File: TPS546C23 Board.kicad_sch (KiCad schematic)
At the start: 35 parts, among them IC1 TPS546C23RVFT

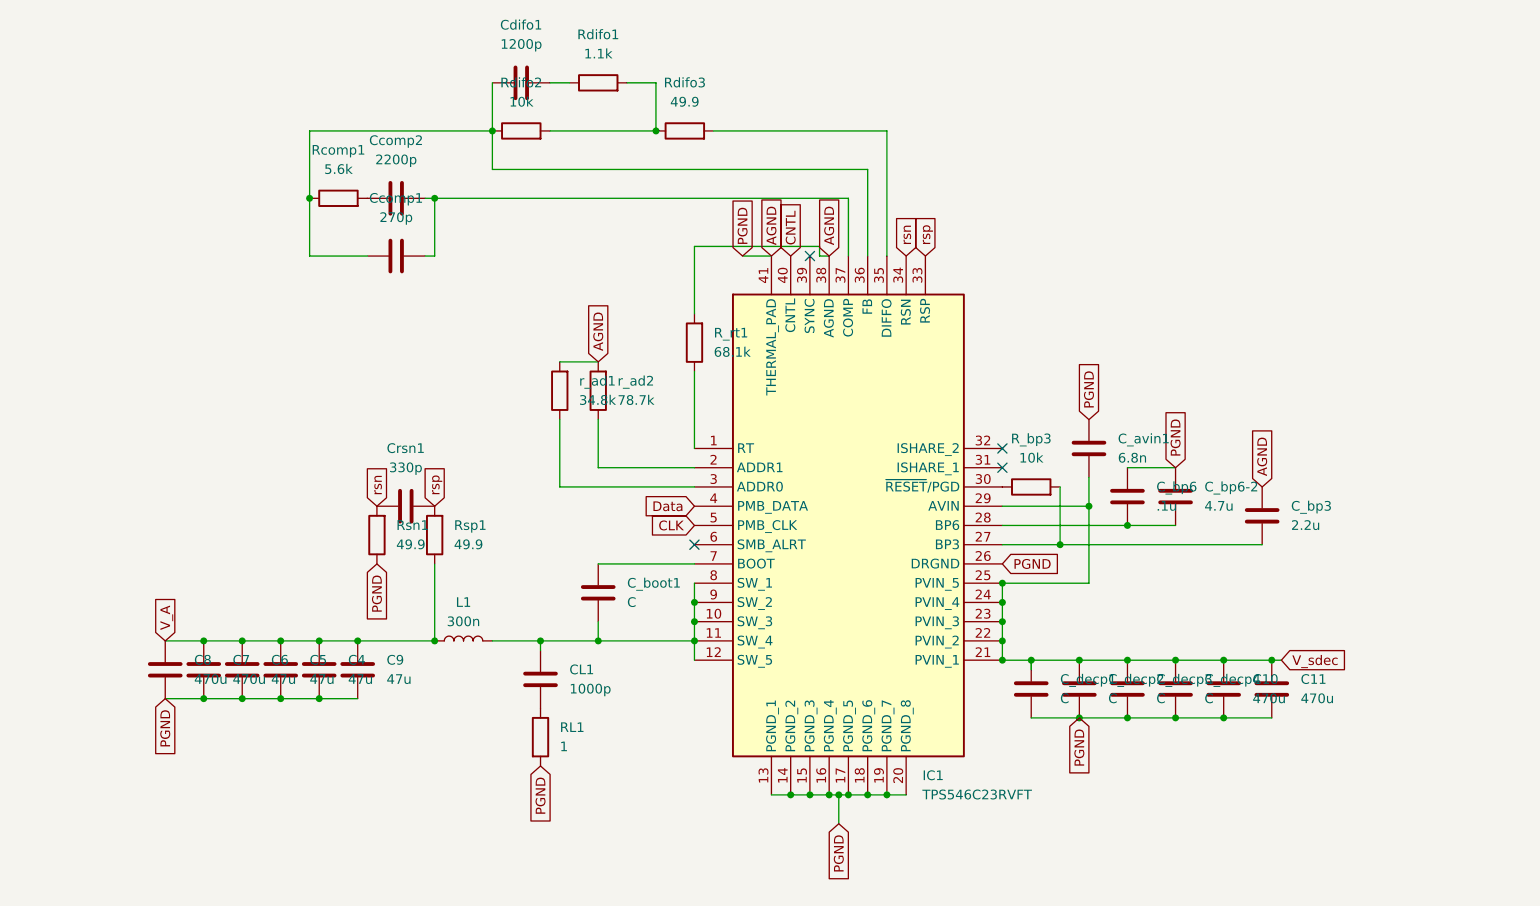
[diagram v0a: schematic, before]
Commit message: add fp and sym, it wasnt final
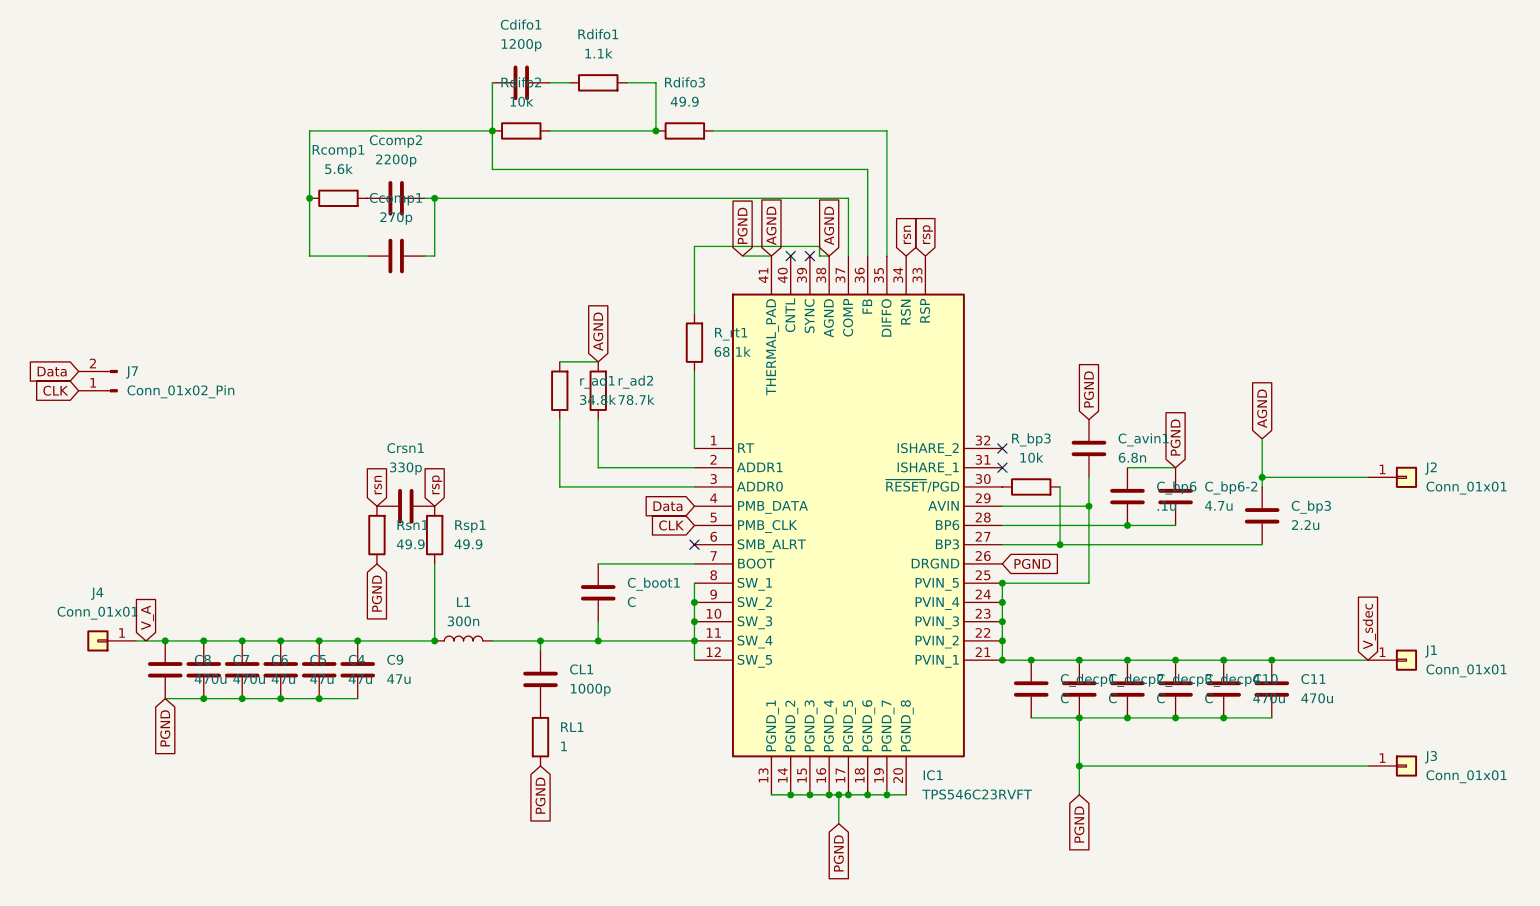
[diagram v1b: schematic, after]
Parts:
- added J1, J2, J3, J4: Conn_01x01, Custom:CalTest_CT3151, symbol Connector_Generic:Conn_01x01
- added J7: Conn_01x02_Pin, Connector_PinHeader_2.54mm:PinHeader_1x02_P2.54mm_Vertical, symbol Connector:Conn_01x02_Pin
- IC1: footprint LIB_TPS546C23RVFT:QFN50P500X700X152-41N-D -> Custom:QFN50P500X700X152-41N-D; symbol highA_highV_buck:TPS546C23RVFT -> TPS546C23RVFT:TPS546C23RVFT
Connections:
- net AGND: now also J2.1 (Pin_1), J3.1 (Pin_1)
- net CLK: now also J7.1 (Pin_1)
- net Data: now also J7.2 (Pin_2)
- net V_A: now also J4.1 (Pin_1)
- net V_sdec: now also J1.1 (Pin_1)
- net CNTL: no longer names the net of IC1.40 (CNTL)
- no-connect marks 4 -> 5
